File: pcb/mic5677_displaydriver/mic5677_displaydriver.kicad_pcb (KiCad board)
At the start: 2 copper layers, 80 parts, among them J1 Segment DIP14, J2 Segment DIP14, J3 H, J4 Sec, J5 Common Cathode Enable, J6 PSU Socket, J7 8P8C, Q1 D45H8G, Q10 BC546, Q11 BC546, Q12 BC546, Q13 BC546, Q14 BC546, Q15 BC546, Q16 BC546, Q17 BC546, Q18 BC546, Q19 BC546, Q2 D45H8G, Q20 BC546, Q21 BC546, Q22 BC546, Q23 BC546, Q3 D45H8G, Q4 D45H8G, Q5 D45H8G, Q6 D45H8G, Q7 D45H8G, Q8 D45H8G, Q9 D45H8G, U1 L7805, U2 74HC595, U3 74HC595, U4 74HC02

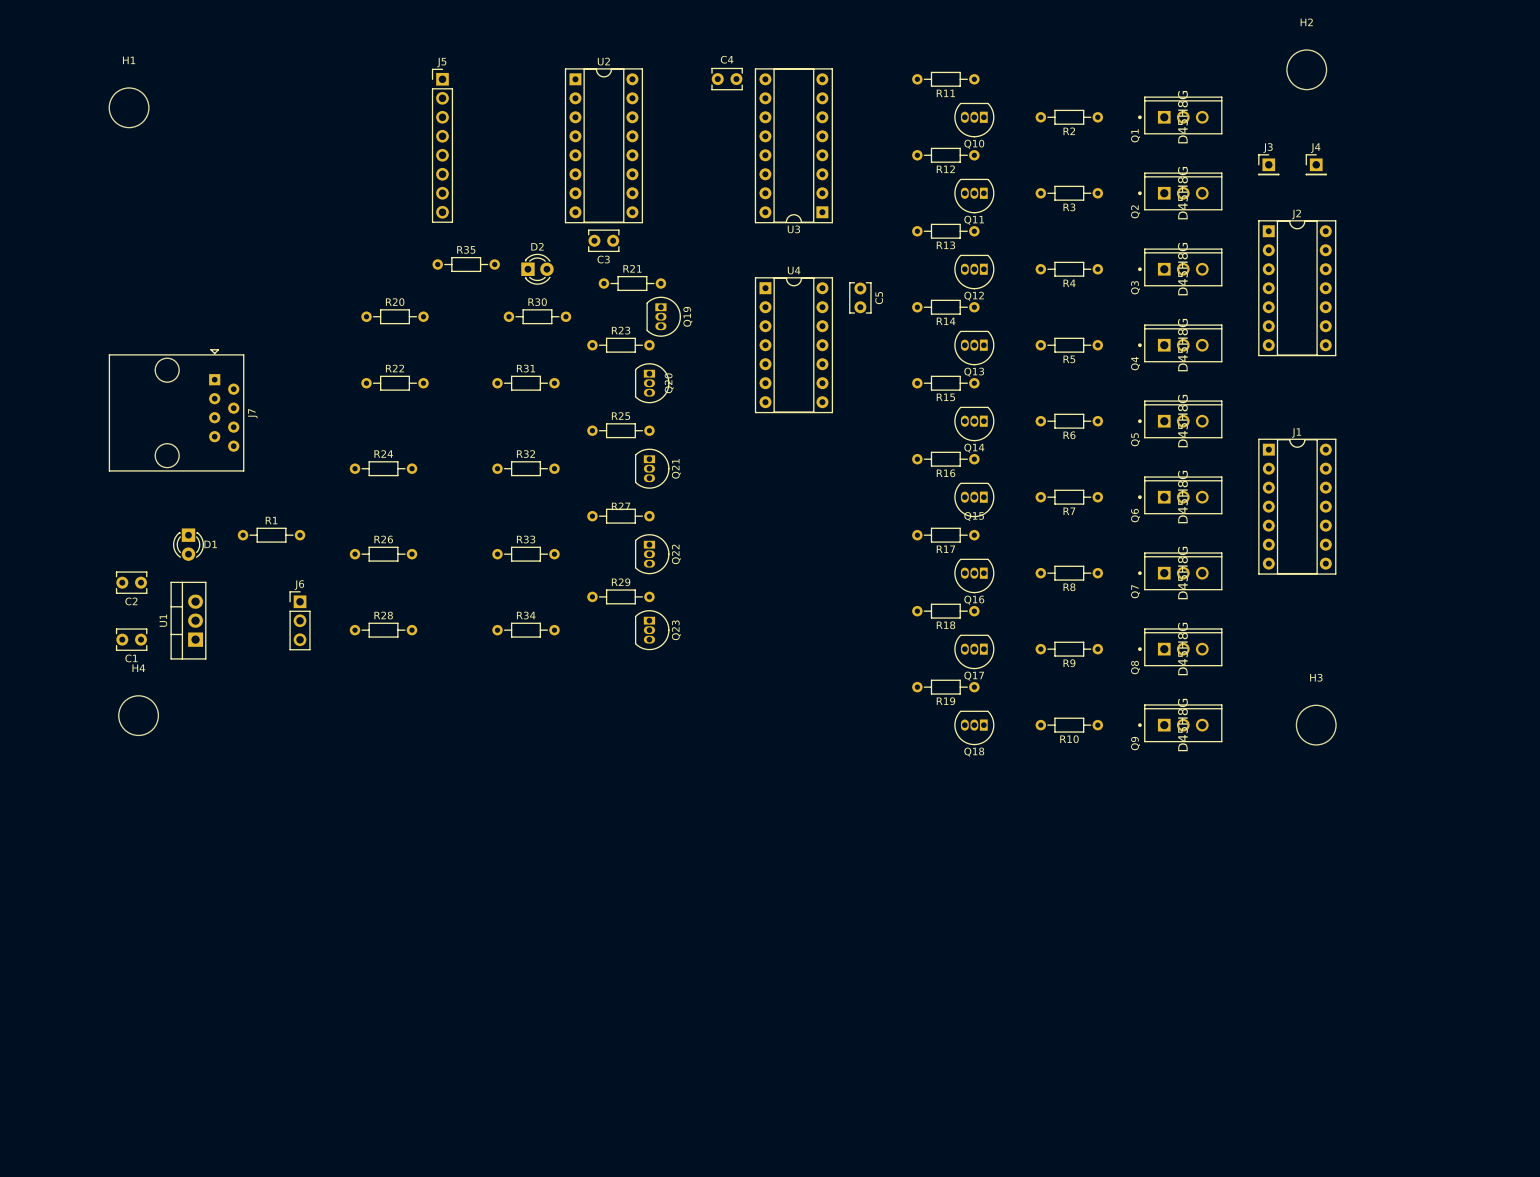
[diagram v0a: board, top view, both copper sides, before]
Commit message: Improved display driver pcb
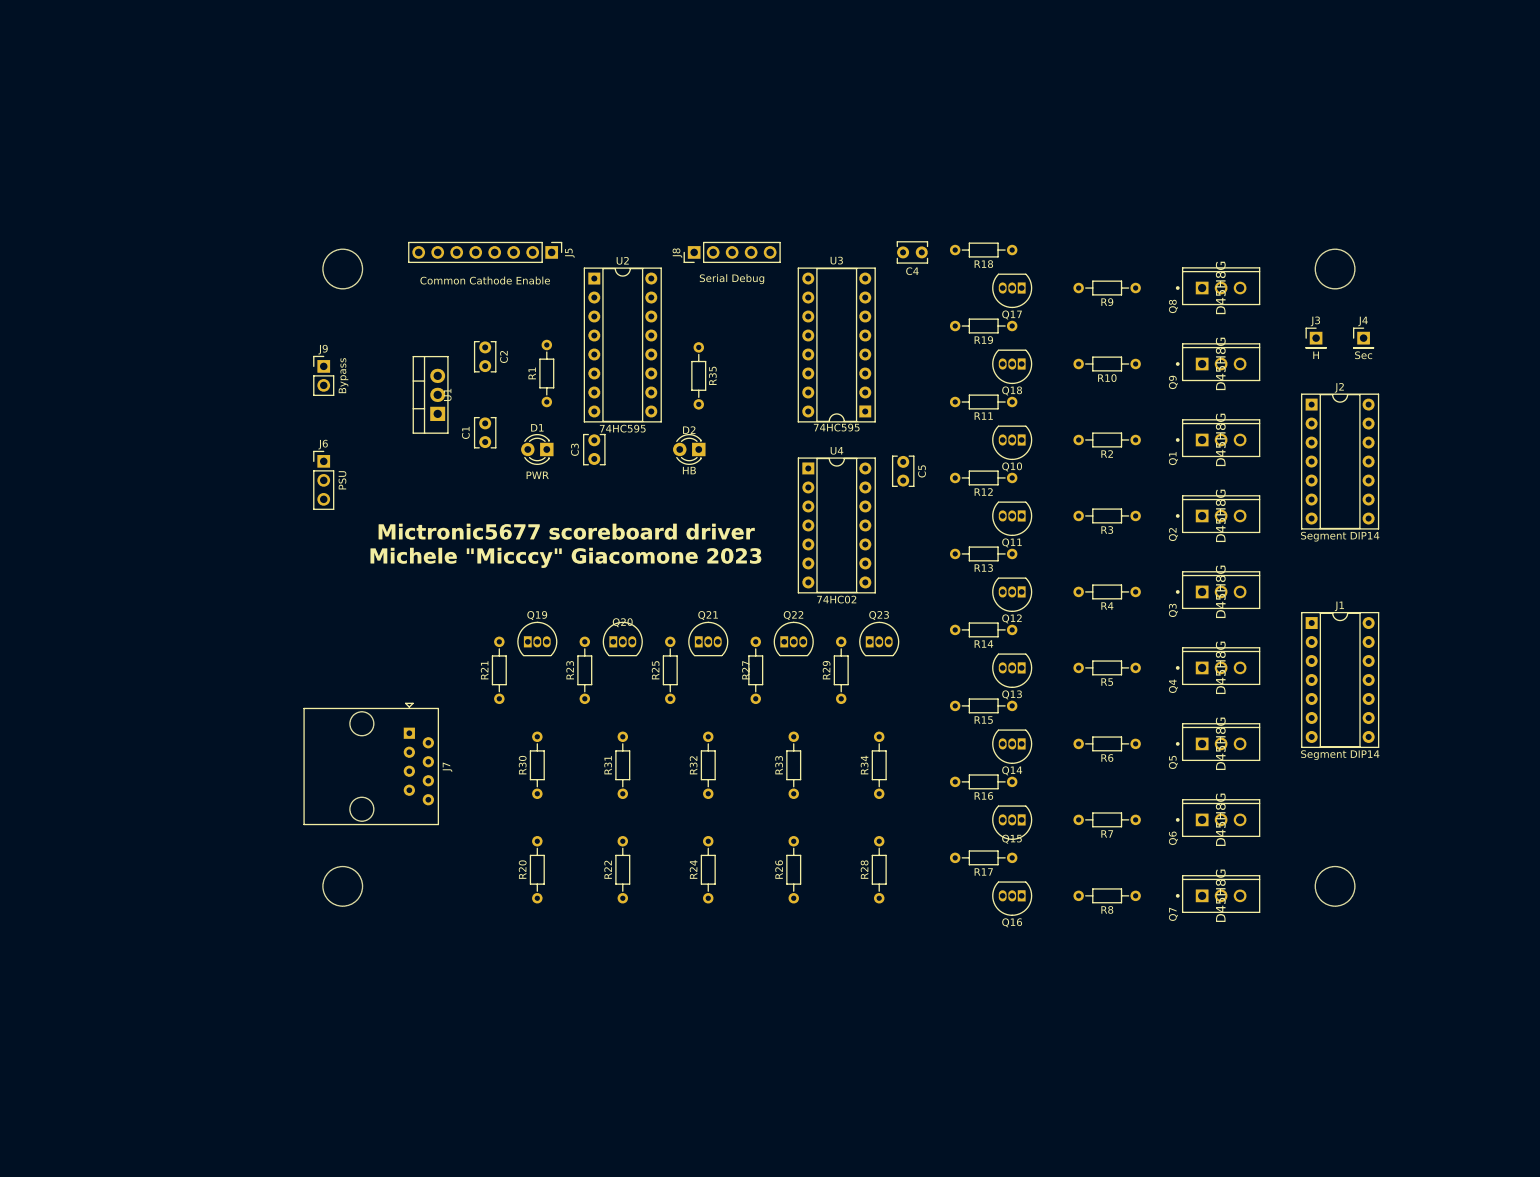
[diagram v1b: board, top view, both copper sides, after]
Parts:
- added J8: Serial Debug, Connector_PinHeader_2.54mm:PinHeader_1x05_P2.54mm_Vertical, F.Cu at (125.1, 40.9)
- added J9: Bypass, Connector_PinHeader_2.54mm:PinHeader_1x02_P2.54mm_Vertical, F.Cu at (75.6, 56.2)
- J6: value PSU Socket -> PSU
- moved R20 81.0 mm to (104.1, 127.3), turned to 90 degrees
- moved R28 78.7 mm to (149.8, 127.3), turned to 90 degrees
- moved R22 76.9 mm to (115.5, 127.3), turned to 90 degrees
- moved R26 74.6 mm to (138.4, 127.3), turned to 90 degrees
- moved R24 74.4 mm to (127.0, 127.3), turned to 90 degrees
- moved R30 63.9 mm to (104.1, 113.3), turned to 90 degrees
- moved R31 57.4 mm to (115.5, 113.3), turned to 90 degrees
- moved R21 57.3 mm to (99.0, 100.6), turned to 90 degrees
- moved C2 55.7 mm to (97.2, 53.6), turned to -90 degrees
- moved R34 55.5 mm to (149.8, 113.3), turned to 90 degrees
- moved J7 54.0 mm to (87.0, 105.2)
- moved C1 53.1 mm to (97.2, 66.3), turned to 90 degrees
- moved R32 51.8 mm to (127.0, 113.3), turned to 90 degrees
- moved R33 51.0 mm to (138.4, 113.3), turned to 90 degrees
- moved D1 49.3 mm to (105.4, 67.3), turned to 180 degrees
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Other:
- board text added: "Mictronic5677 scoreboard driver Michele {dblquote}Micccy{dblquote} Giacomone 2023"

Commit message: Finished display driver pcb
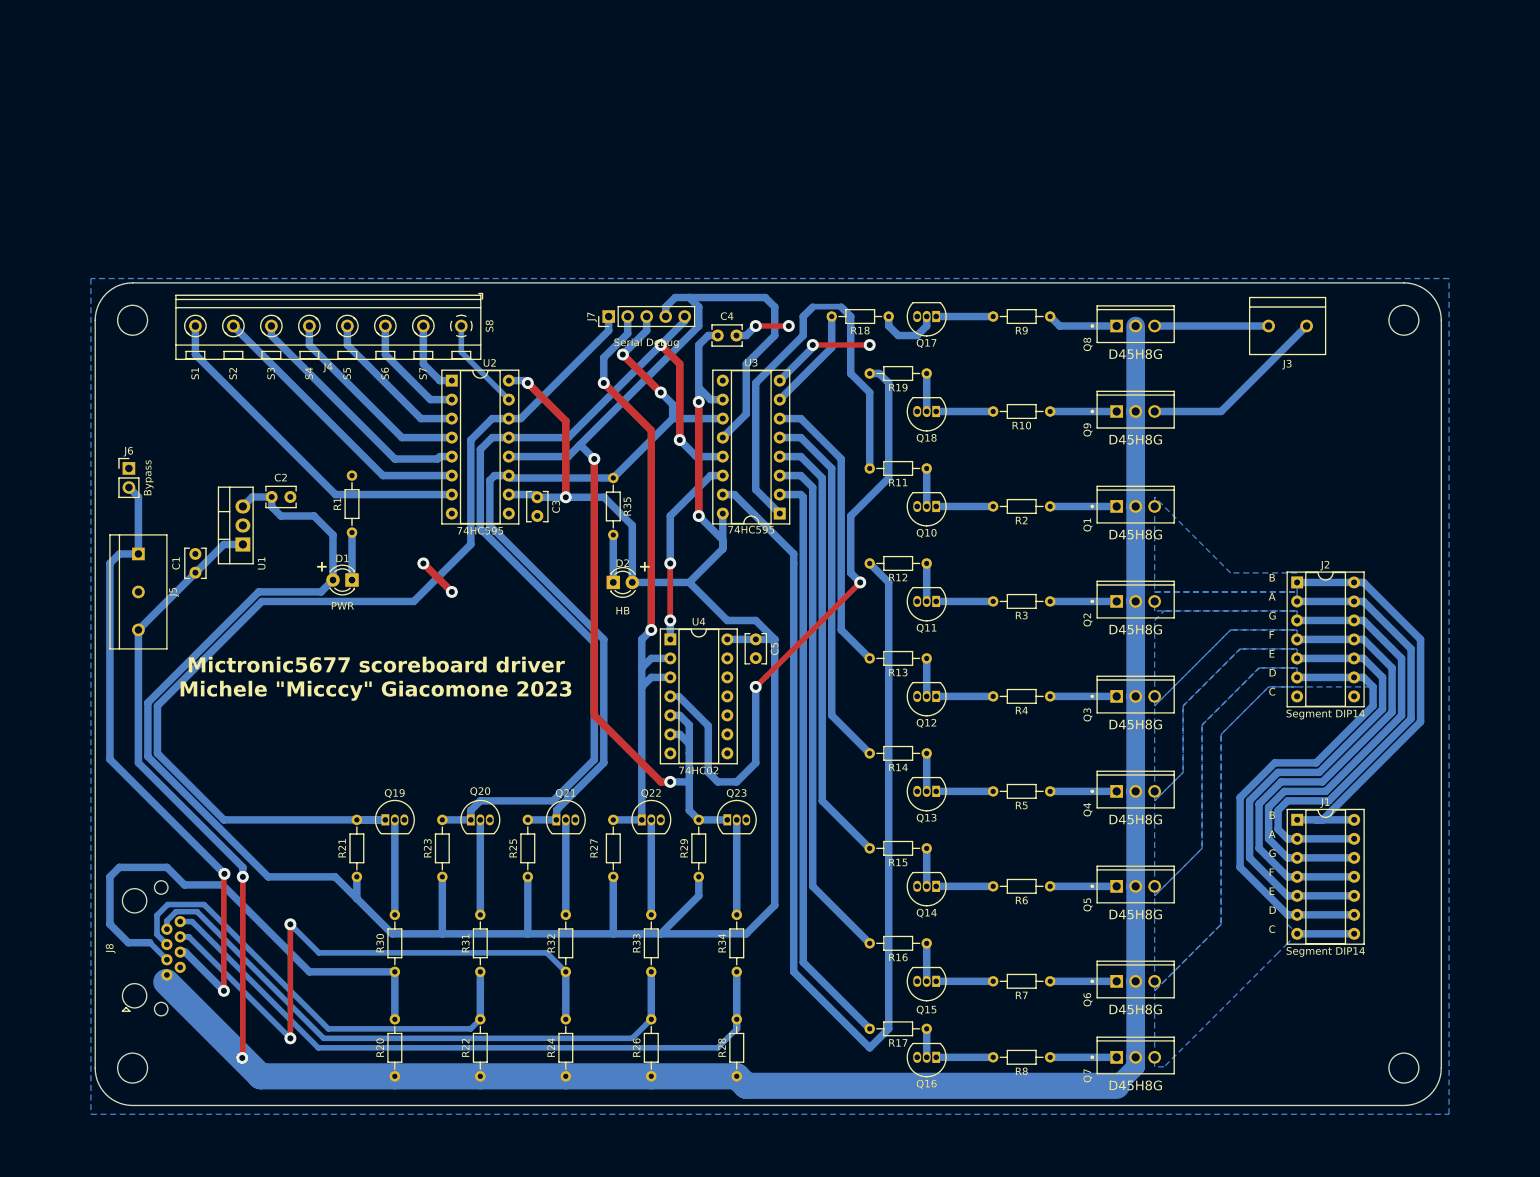
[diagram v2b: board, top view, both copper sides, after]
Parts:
- removed the J6 at (75.6, 68.9)
- H1, H2, H3, H4: value MountingHole -> 4mm; footprint MountingHole:MountingHole_5.3mm_M5 -> MountingHole:MountingHole_4mm
- J3: value H -> Segment Wire Connector; footprint Connector_PinHeader_2.54mm:PinHeader_1x01_P2.54mm_Vertical -> TerminalBlock:TerminalBlock_bornier-2_P5.08mm
- J4: value Sec -> Common Cathode Enable; footprint Connector_PinHeader_2.54mm:PinHeader_1x01_P2.54mm_Vertical -> TerminalBlock_RND:TerminalBlock_RND_205-00238_1x08_P5.08mm_Horizontal
- J5: value Common Cathode Enable -> PSU; footprint Connector_PinHeader_2.54mm:PinHeader_1x08_P2.54mm_Vertical -> TerminalBlock:TerminalBlock_bornier-3_P5.08mm
- moved J4 120.7 mm to (94.0, 50.8), turned to 180 degrees
- moved J5 68.4 mm to (50.8, 81.2)
- moved J8 50.3 mm to (49.1, 138.4), turned to 90 degrees
- moved C1 42.5 mm to (58.4, 83.8)
- moved H4 37.1 mm to (50.0, 150.0)
- moved C2 34.9 mm to (68.6, 73.6), turned to 0 degrees
- moved R1 31.4 mm to (79.3, 78.4)
- moved U1 31.4 mm to (64.8, 80.0)
- moved D1 31.4 mm to (79.3, 84.7)
- moved C5 30.9 mm to (133.3, 92.7)
- moved R21 30.5 mm to (80.0, 124.4)
- moved R25 30.5 mm to (102.8, 124.4)
- moved R27 30.5 mm to (114.3, 124.4)
- moved R30 30.5 mm to (85.1, 137.1)
- moved R34 30.5 mm to (130.8, 137.1)
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- renumbered J9 to J6, J8 to J7, J7 to J8
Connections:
- net Net-(J1-Pin_1) renamed /B_OUT
- net Net-(J1-Pin_10) renamed /E_OUT
- net Net-(J1-Pin_11) renamed /F_OUT
- net Net-(J1-Pin_12) renamed /G_OUT
- net Net-(J1-Pin_13) renamed /A_OUT
- net Net-(J1-Pin_6) renamed /D_OUT
- net Net-(J1-Pin_7) renamed /C_OUT
- net Net-(J3-Pin_1) renamed /H_OUT
- J4 pad 1: Net-(J4-Pin_1) -> /S8
- J5 pad 1: /S8 -> /PWR_EN
- J5 pad 2: /S7 -> GND
- J5 pad 3: /S6 -> VDC
- Q9 pad 3: Net-(J4-Pin_1) -> /SEC_OUT
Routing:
- net +5V: track 0.00 -> 347.5 mm, vias 0 -> 4
- net VDC: track 0.00 -> 317.2 mm, vias 0 -> 2
- net RCLK: track 0.00 -> 150.7 mm, vias 0 -> 2
- net A: track 0.00 -> 149.9 mm
- net SER1: track 0.00 -> 135.5 mm
- net OE: track 0.00 -> 127.7 mm, vias 0 -> 2
- net SRCLK: track 0.00 -> 110.7 mm, vias 0 -> 2
- net /RCLK_IN: track 0.00 -> 90.1 mm
- net /PWR_EN: track 0.00 -> 85.3 mm, vias 0 -> 2
- net SER0: track 0.00 -> 84.3 mm, vias 0 -> 2
- net SEC: track 0.00 -> 83.1 mm, vias 0 -> 2
- net /SRCLK_IN: track 0.00 -> 81.4 mm, vias 0 -> 2
- net /SER0_IN: track 0.00 -> 80.8 mm
- net C: track 0.00 -> 78.1 mm
- net D: track 0.00 -> 69.2 mm
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- added copper zone on B.Cu, net /A_OUT
- added copper zone on B.Cu, net /B_OUT
- added copper zone on B.Cu, net /C_OUT
- added copper zone on B.Cu, net /D_OUT
- added copper zone on B.Cu, net /E_OUT
- added copper zone on B.Cu, net /F_OUT
- added copper zone on B.Cu, net /G_OUT
- added copper zone on B.Cu, net GND
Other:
- board outline added: 180 x 110 mm
- board text added: "+"
- board text added: "A"
- board text added: "B"
- board text added: "C"
- board text added: "D"
- board text added: "E"
- board text added: "F"
- board text added: "G"
- board text added: "S1"
- board text added: "S2"
- board text added: "S3"
- board text added: "S4"
- board text added: "S5"
- board text added: "S6"
- board text added: "S7"
- board text added: "S8"

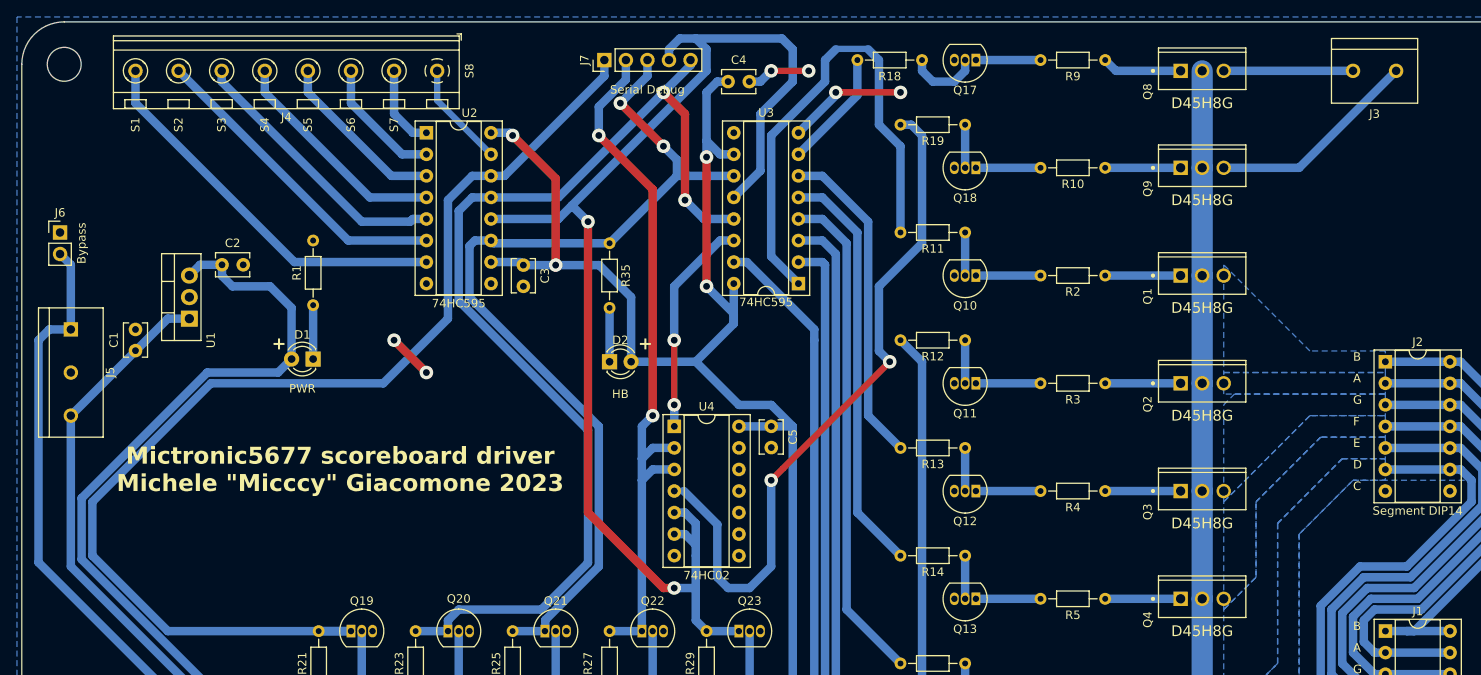
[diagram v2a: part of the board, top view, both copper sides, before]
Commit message: Added some silkscreen on pcb and changed io style
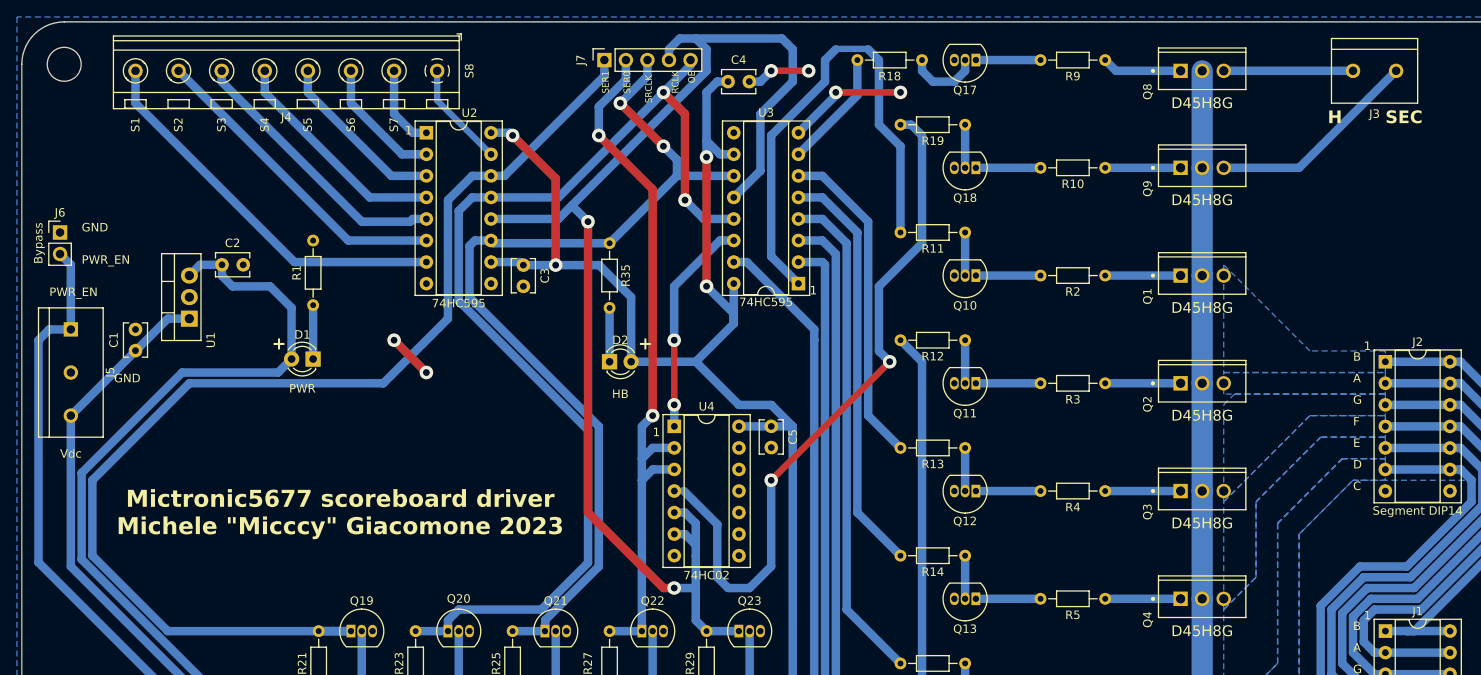
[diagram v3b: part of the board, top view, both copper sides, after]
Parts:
- J7: footprint Connector_PinHeader_2.54mm:PinHeader_1x05_P2.54mm_Vertical -> Connector_PinSocket_2.54mm:PinSocket_1x05_P2.54mm_Vertical
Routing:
- net +5V: track 347.5 -> 349.3 mm
- net SER1: track 135.5 -> 137.0 mm
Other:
- board text added: "1"
- board text added: "GND"
- board text added: "H"
- board text added: "OE"
- board text added: "PWR_EN"
- board text added: "RCLK"
- board text added: "SEC"
- board text added: "SER0"
- board text added: "SER1"
- board text added: "SRCLK"
- board text added: "Vdc"
